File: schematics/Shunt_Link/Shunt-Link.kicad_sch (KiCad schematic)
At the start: 17 parts, among them IC1 AD8221TRMZ-EP, IC2 AD8221TRMZ-EP, IC3 AD8244ARMZ, J1 PCIe_1x_Bus, J2 Conn_01x05_Socket

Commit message: Updated to git
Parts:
- removed D1: LED_Lights, APT_Needs:LED_Lights, symbol APT_Needs:LED_Lights
- removed IC1, IC2: AD8221TRMZ-EP, APT_Needs:AD8221TRMZ-EP, symbol APT_Needs:AD8221TRMZ-EP
- removed IC3: AD8244ARMZ, APT_Needs:AD8244ARMZ, symbol APT_Needs:AD8244ARMZ
- removed J1: PCIe_1x_Bus, Connector_PCBEdge:BUS_PCIexpress_x1, symbol APT_Needs:PCIe_1x_Bus
- removed TP1, TP2, TP3: Keystone_1045, APT_Needs:Keystone_1045, symbol APT_Needs:Keystone_1045
- added D1: WP130WCP_2EGW, Link_Footprints:LED_Lights, symbol Link_Components:WP130WCP_2EGW
- added IC1, IC2: AD8221TRMZ-EP, Link_Footprints:AD8221TRMZ-EP, symbol Link_Components:AD8221TRMZ-EP
- added J1: PCIE-036-02-X-D-TH, Link_Footprints:SAMTEC_PCIE_1x, symbol Link_Components:PCIE-036-02-X-D-TH
- added L1: AD8244ARMZ, Link_Footprints:AD8244ARMZ, symbol Link_Components:AD8244ARMZ
- added TP1, TP2, TP3: 1045, Link_Footprints:Keystone_1045, symbol Link_Components:1045
- J2: footprint APT_Needs:Phoenix_Contact_MSTBA-LR -> Link_Footprints:Phoenix_Contact_MSTBA,5-LR
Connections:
- net GND: now also D1.2, D1.5, IC1.4 (+IN), IC1.5 (-VS), IC2.4 (+IN), IC2.5 (-VS), J1.B18, L1.8 (-VS), TP3.TP1
- net Green_{1}: now also D1.3, J1.B10
- net Green_{2}: now also D1.6, J1.B12
- net Red_{1}: now also D1.1, J1.B11
- net Red_{2}: now also D1.4, J1.B13
- net S_{+}: now also IC1.1 (-IN)
- net S_{o}: now also IC1.7 (VOUT), J1.B1, L1.6 (INC)
- net S_{test}: now also L1.7 (OUTC), TP1.TP1
- net T_{+}: now also IC2.1 (-IN)
- net T_{o}: now also IC2.7 (VOUT), J1.B2, L1.10 (IND)
- net T_{test}: now also L1.9 (OUTD), TP2.TP1
- net V_{+}: now also L1.4 (OUTB)
- net V_{2.5}: now also L1.1 (INA)
- net V_{5}: now also L1.5 (INB)
- net V_{ref}: now also IC1.6 (REF), IC2.6 (REF), L1.2 (OUTA)
- net V_{s}: now also IC1.8 (+VS), IC2.8 (+VS), J1.B17, L1.3 (+VS)
- net at Rg_2.1: now also IC2.2 (RG_1)
- net at Rg_2.2: now also IC2.3 (RG_2)
- net at Rg_1.1: now also IC1.2 (RG_1)
- net at Rg_1.2: now also IC1.3 (RG_2)
- new net NC: J1.A1, J1.A10, J1.A11, J1.A12, J1.A13, J1.A14, J1.A15, J1.A16, J1.A17, J1.A18, J1.A2, J1.A3, J1.A4, J1.A5, J1.A6, J1.A7, J1.A8, J1.A9, J1.B14, J1.B15, J1.B16, J1.B3, J1.B4, J1.B5, J1.B6, J1.B7, J1.B8, J1.B9

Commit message: started straing gauge link, updated shunt-link:
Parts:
- added C1: 0.1 uF, symbol Device:C
- added C2: 10 uF, symbol Device:C_US
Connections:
- net GND: now also C1.2, C2.2
- net V_{s}: now also C1.1, C2.1
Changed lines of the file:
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@@
 	(paper "A4")
+	(junction
+		(at 151.13 31.75)
+		(diameter 0)
+		(color 0 0 0 0)
+	)
 	(junction
 		(at 85.09 39.37)
@@
 	)
 	(junction
+		(at 165.1 31.75)
+		(diameter 0)
+		(color 0 0 0 0)
+	)
+	(junction
 		(at 93.98 118.11)
+		(diameter 0)
+		(color 0 0 0 0)
+	)
+	(junction
+		(at 151.13 39.37)
+		(diameter 0)
+		(color 0 0 0 0)
+	)
+	(junction
+		(at 165.1 39.37)
 		(diameter 0)
 		(color 0 0 0 0)
@@
 	(wire
 		(pts
-			(xy 132.08 39.37) (xy 138.43 39.37)
-		)
-		(stroke
-			(width 0)
-			(type default)
-		)
-	)
-	(wire
-		(pts
 			(xy 147.32 134.62) (xy 152.4 134.62)
 		)
@@
 	(wire
 		(pts
+			(xy 172.72 39.37) (xy 165.1 39.37)
+		)
+		(stroke
+			(width 0)
+			(type default)
+		)
+	)
+	(wire
+		(pts
 			(xy 73.66 40.64) (xy 85.09 40.64)
 		)
@@
 	(wire
 		(pts
+			(xy 151.13 31.75) (xy 165.1 31.75)
+		)
+		(stroke
+			(width 0)
+			(type default)
+		)
+	)
+	(wire
+		(pts
 			(xy 86.36 54.61) (xy 86.36 53.34)
 		)
@@
 	(wire
 		(pts
+			(xy 132.08 31.75) (xy 151.13 31.75)
+		)
+		(stroke
+			(width 0)
+			(type default)
+		)
+	)
+	(wire
+		(pts
 			(xy 76.2 118.11) (xy 76.2 120.65)
 		)
@@
 	(wire
 		(pts
+			(xy 132.08 39.37) (xy 151.13 39.37)
+		)
+		(stroke
+			(width 0)
+			(type default)
+		)
+	)
+	(wire
+		(pts
 			(xy 102.87 36.83) (xy 104.14 36.83)
 		)
@@
 	(wire
 		(pts
+			(xy 165.1 39.37) (xy 151.13 39.37)
+		)
+		(stroke
+			(width 0)
+			(type default)
+		)
+	)
+	(wire
+		(pts
 			(xy 116.84 111.76) (xy 121.92 111.76)
 		)
@@
 	(wire
 		(pts
+			(xy 165.1 31.75) (xy 172.72 31.75)
+		)
+		(stroke
+			(width 0)
+			(type default)
+		)
+	)
+	(wire
+		(pts
 			(xy 116.84 114.3) (xy 121.92 114.3)
 		)
@@
 	(wire
 		(pts
-			(xy 132.08 31.75) (xy 138.43 31.75)
-		)
-		(stroke
-			(width 0)
-			(type default)
-		)
-	)
-	(wire
-		(pts
 			(xy 93.98 118.11) (xy 93.98 120.65)
 		)
@@
 	(label "NC"
 		(at 116.84 129.54 0)
+		(effects
+			(font
+				(size 1.27 1.27)
+			)
+			(justify left bottom)
+		)
+	)
+	(label "GND"
+		(at 172.72 39.37 0)
 		(effects
 			(font
@@
 		)
 	)
+	(label "V_{s}"
+		(at 172.72 31.75 0)
+		(effects
+			(font
+				(size 1.27 1.27)
+			)
+			(justify left bottom)
+		)
+	)
 	(label "T_{test}"
 		(at 139.7 78.74 0)
@@
 		)
 	)
-	(label "GND"
-		(at 138.43 39.37 0)
-		(effects
-			(font
-				(size 1.27 1.27)
-			)
-			(justify left bottom)
-		)
-	)
 	(label "NC"
 		(at 116.84 121.92 0)
-		(effects
-			(font
-				(size 1.27 1.27)
-			)
-			(justify left bottom)
-		)
-	)
-	(label "V_{s}"
-		(at 138.43 31.75 0)
 		(effects
 			(font
@@
 			)
 			(justify left bottom)
+		)
+	)
+	(symbol
+		(lib_id "Device:C_US")
+		(at 165.1 35.56 0)
+		(unit 1)
+		(exclude_from_sim no)
+		(in_bom yes)
+		(on_board yes)
+		(dnp no)
+		(property "Reference" "C2"
+			(at 168.91 33.528 0)
+			(effects
+				(font
+					(size 1.27 1.27)
+				)
+				(justify left)
+			)
+		)
+		(property "Value" "10 uF"
+			(at 168.91 36.068 0)
+			(effects
+				(font
+					(size 1.27 1.27)
+				)
+				(justify left)
+			)
+		)
+		(property "Footprint" ""
+			(at 165.1 35.56 0)
+			(effects
+				(font
+					(size 1.27 1.27)
+				)
+				(hide yes)
+			)
+		)
+		(property "Datasheet" ""
+			(at 165.1 35.56 0)
+			(effects
+				(font
+					(size 1.27 1.27)
+				)
+				(hide yes)
+			)
+		)
+		(property "Description" "capacitor, US symbol"
+			(at 165.1 35.56 0)
+			(effects
+				(font
+					(size 1.27 1.27)
+				)
+				(hide yes)
+			)
+		)
+		(pin "1"
+		)
+		(pin "2"
+		)
+		(instances
+			(project "Shunt-Link"
+				(path "/044df771-0288-4dc4-a604-257e905d1378"
+					(reference "C2")
+					(unit 1)
+				)
+			)
 		)
 	)
@@
 					(unit 1)
 				)
+			)
+		)
+	)
+	(symbol
+		(lib_id "Device:C")
+		(at 151.13 35.56 0)
+		(unit 1)
+		(exclude_from_sim no)
+		(in_bom yes)
+		(on_board yes)
+		(dnp no)
+		(fields_autoplaced yes)
+		(property "Reference" "C1"
+			(at 154.94 34.2899 0)
+			(effects
+				(font
+					(size 1.27 1.27)
+				)
+				(justify left)
+			)
+		)
+		(property "Value" "0.1 uF"
+			(at 154.94 36.8299 0)
+			(effects
+				(font
+					(size 1.27 1.27)
+				)
+				(justify left)
+			)
+		)
+		(property "Footprint" ""
+			(at 152.0952 39.37 0)
+			(effects
+				(font
+					(size 1.27 1.27)
+				)
+				(hide yes)
+			)
+		)
+		(property "Datasheet" "~"
+			(at 151.13 35.56 0)
+			(effects
+				(font
+					(size 1.27 1.27)
+				)
+				(hide yes)
+			)
+		)
+		(property "Description" "Unpolarized capacitor"
+			(at 151.13 35.56 0)
+			(effects
+				(font
+					(size 1.27 1.27)
+				)
+				(hide yes)
+			)
+		)
+		(pin "2"
+		)
+		(pin "1"
+		)
+		(instances
+			(project "Shunt-Link"
+				(path "/044df771-0288-4dc4-a604-257e905d1378"
+					(reference "C1")
+					(unit 1)
+				)

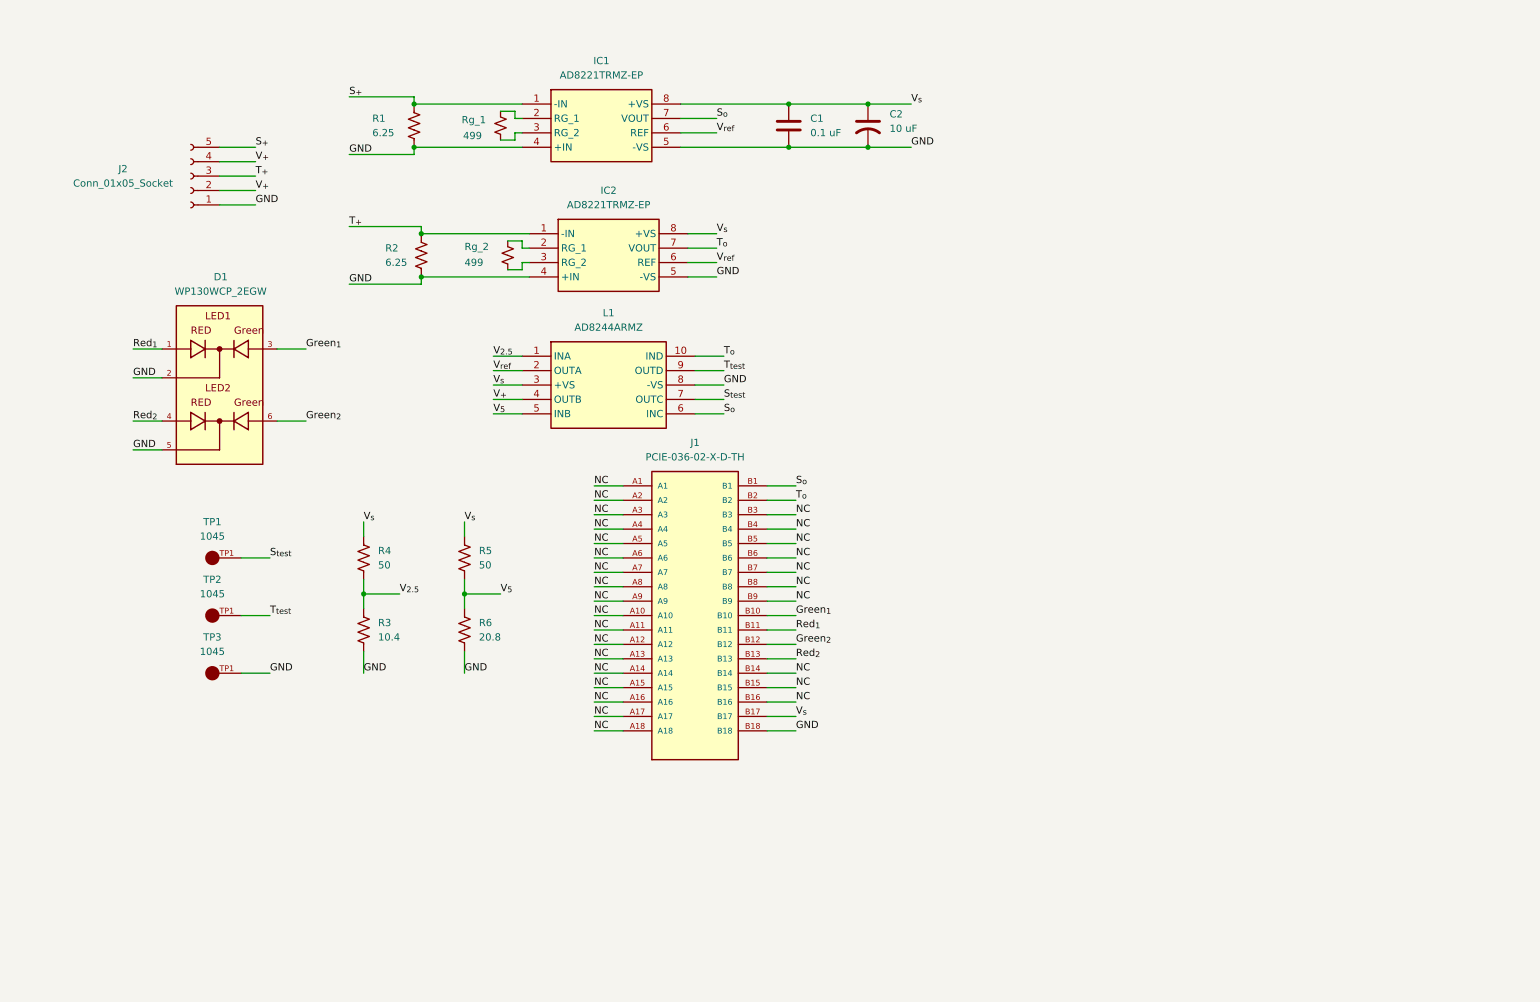
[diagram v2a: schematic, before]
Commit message: Changed V Labels, remove extra pins for now
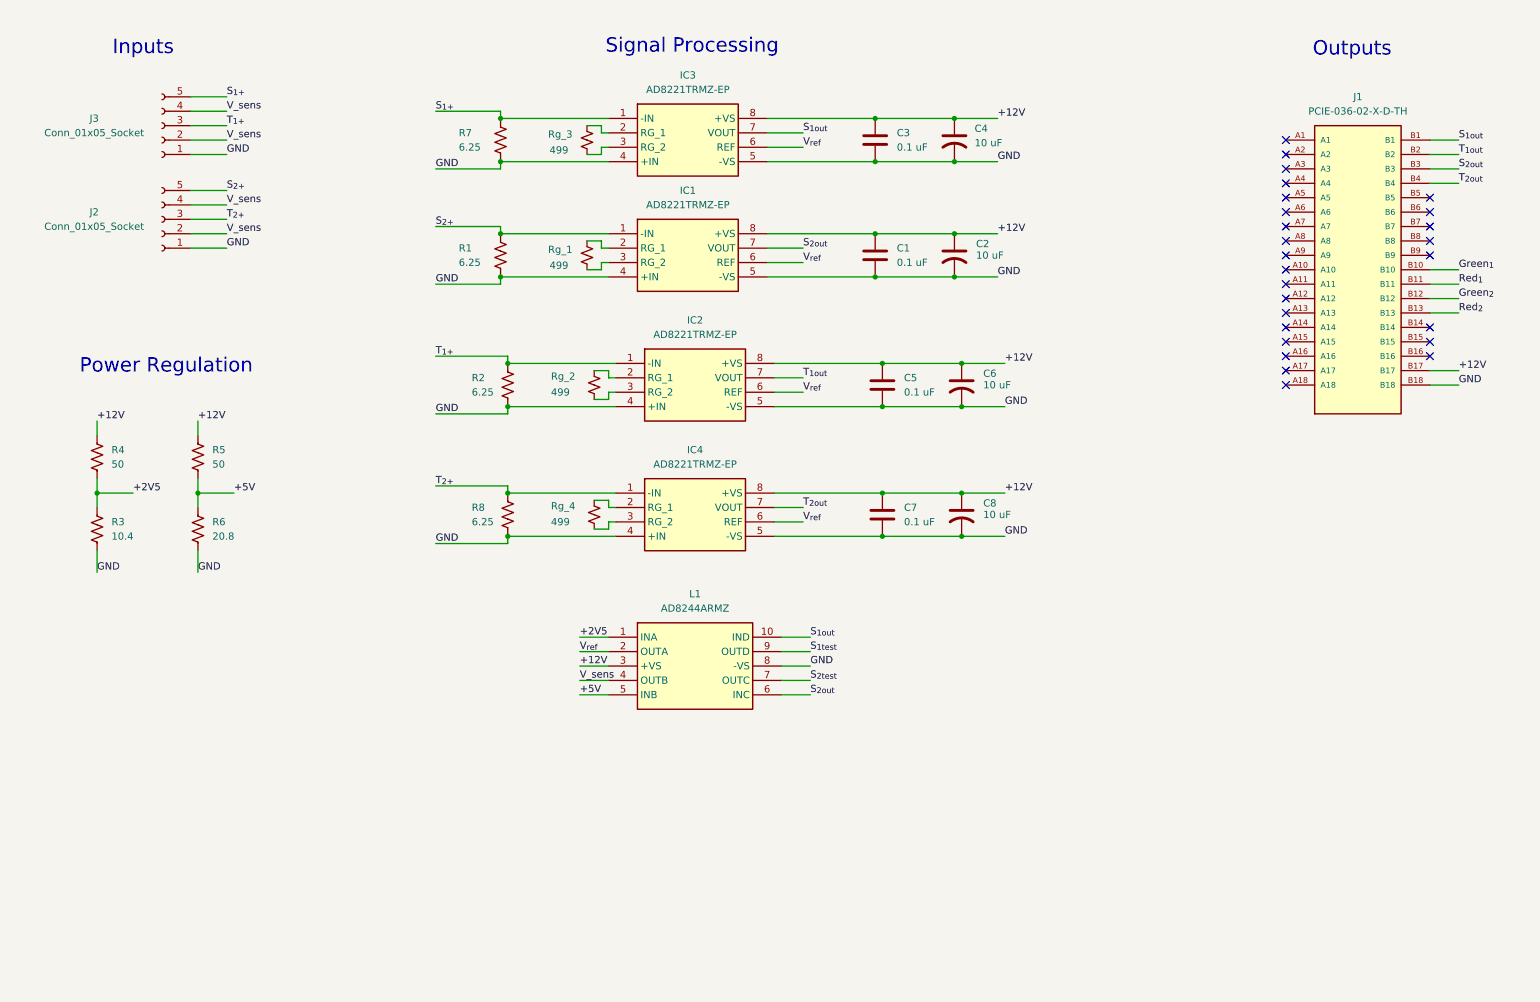
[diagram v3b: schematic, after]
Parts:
- removed D1: WP130WCP_2EGW, Link_Footprints:LED_Lights, symbol Link_Components:WP130WCP_2EGW
- removed TP1, TP2, TP3: 1045, Link_Footprints:Keystone_1045, symbol Link_Components:1045
- added C3, C5, C7: 0.1 uF, Capacitor_SMD:C_1210_3225Metric, symbol Device:C
- added C4, C6, C8: 10 uF, Capacitor_SMD:C_1210_3225Metric, symbol Device:C_US
- added IC3, IC4: AD8221TRMZ-EP, Link_Footprints:AD8221TRMZ-EP, symbol Link_Components:AD8221TRMZ-EP
- added J3: Conn_01x05_Socket, Link_Footprints:Phoenix_Contact_MSTBA,5-LR, symbol Connector:Conn_01x05_Socket
- added R7, R8: 6.25, Resistor_SMD:R_0805_2012Metric, symbol Device:R_US
- added Rg_3, Rg_4: 499, Resistor_SMD:R_0805_2012Metric, symbol Device:R_Small_US
- C1, C2: footprint (none) -> Capacitor_SMD:C_1210_3225Metric
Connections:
- net GND: now also C3.2, C4.2, C5.2, C6.2, C7.2, C8.2, IC3.4 (+IN), IC3.5 (-VS), IC4.4 (+IN), IC4.5 (-VS), J3.1 (Pin_1), R7.2, R8.2
- net V_{ref}: now also IC3.6 (REF), IC4.6 (REF)
- removed net NC: J1.A1, J1.A10, J1.A11, J1.A12, J1.A13, J1.A14, J1.A15, J1.A16, J1.A17, J1.A18, J1.A2, J1.A3, J1.A4, J1.A5, J1.A6, J1.A7, J1.A8, J1.A9, J1.B14, J1.B15, J1.B16, J1.B3, J1.B4, J1.B5, J1.B6, J1.B7, J1.B8, J1.B9
- net S_{+} renamed S_{2+}
- net S_{o} renamed S_{2out}
- net S_{2out}: now also J1.B3; no longer J1.B1
- net S_{test} renamed S_{2test}
- net T_{+} renamed T_{1+}
- net T_{1+}: now also J3.3 (Pin_3); no longer J2.3 (Pin_3)
- net T_{o} renamed T_{1out}
- net T_{1out}: no longer L1.10 (IND)
- net T_{test} renamed S_{1test}
- net V_{+} renamed V_sens
- net V_sens: now also J3.2 (Pin_2), J3.4 (Pin_4)
- net V_{2.5} renamed +2V5
- net V_{5} renamed +5V
- net V_{s} renamed +12V
- net +12V: now also C3.1, C4.1, C5.1, C6.1, C7.1, C8.1, IC3.8 (+VS), IC4.8 (+VS)
- new net: IC3.2 (RG_1), Rg_3.1
- new net: IC3.3 (RG_2), Rg_3.2
- new net: IC4.2 (RG_1), Rg_4.1
- new net: IC4.3 (RG_2), Rg_4.2
- new net S_{1+}: IC3.1 (-IN), J3.5 (Pin_5), R7.1
- new net S_{1out}: IC3.7 (VOUT), J1.B1, L1.10 (IND)
- new net T_{2+}: IC4.1 (-IN), J2.3 (Pin_3), R8.1
- new net T_{2out}: IC4.7 (VOUT), J1.B4
- no-connect marks 0 -> 26
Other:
- note added: "Inputs"
- note added: "Outputs"
- note added: "Power Regulation"
- note added: "Signal Processing"
- moved on the sheet: C1, C2, IC1, IC2, J1, J2, L1, R1, R2, R3, R4, R5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

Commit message: Added regulators to Shunt_Link, Edited lib
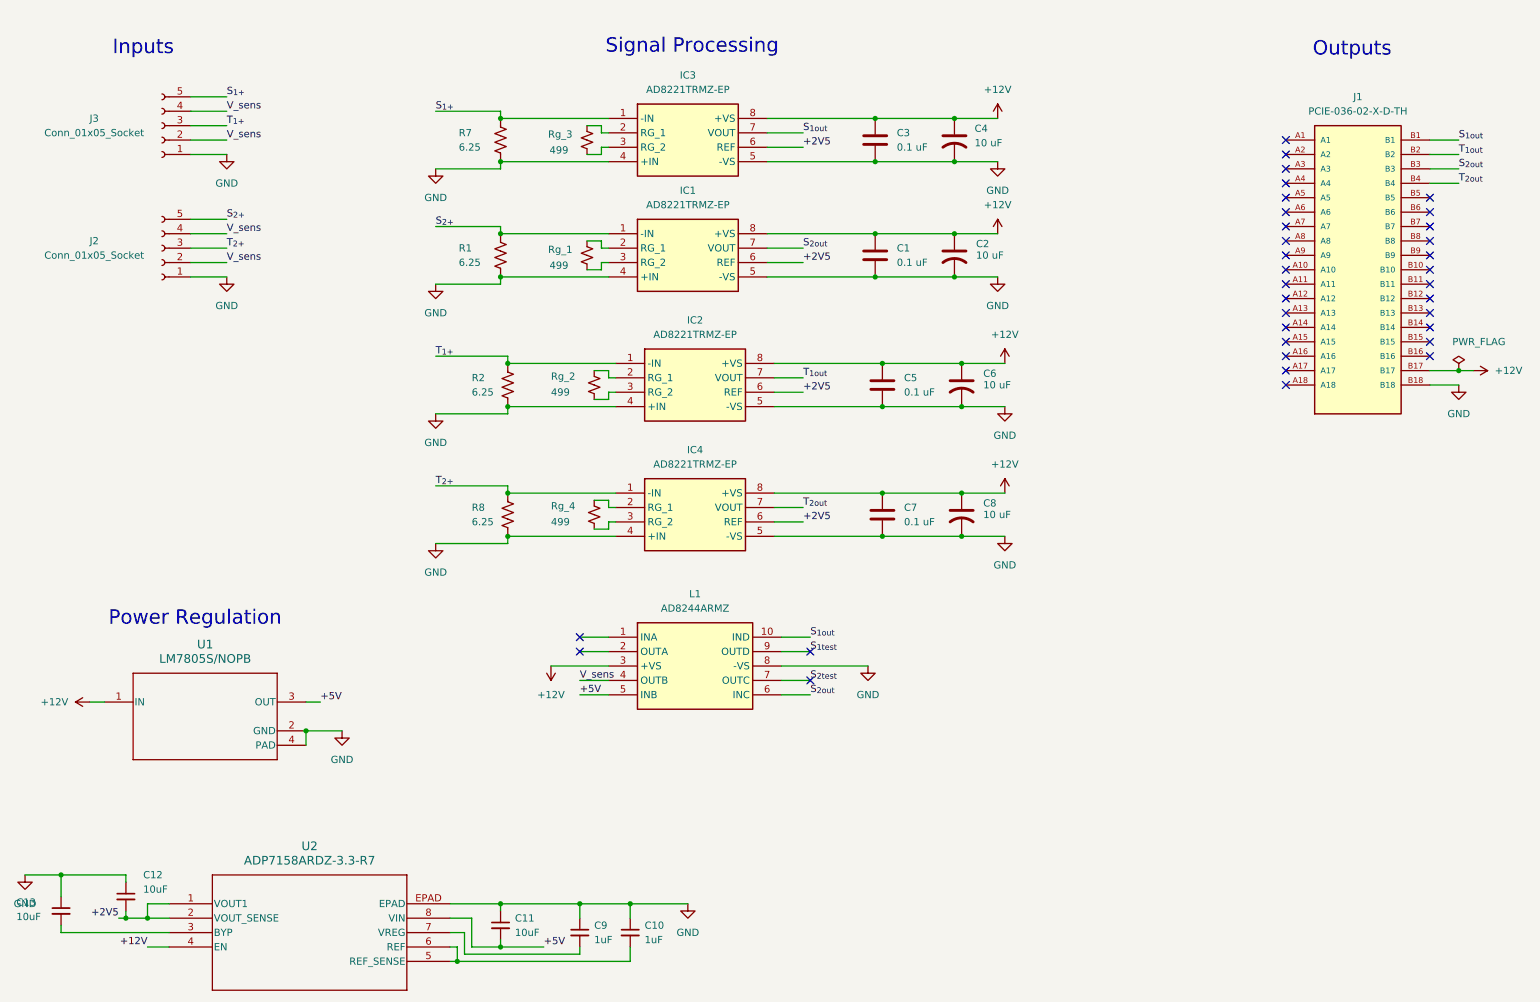
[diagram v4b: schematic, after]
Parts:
- removed R3: 10.4, Resistor_SMD:R_0805_2012Metric, symbol Device:R_US
- removed R4, R5: 50, Resistor_SMD:R_0805_2012Metric, symbol Device:R_US
- removed R6: 20.8, Resistor_SMD:R_0805_2012Metric, symbol Device:R_US
- added C10, C9: 1uF, symbol Device:C_Small
- added C11, C12, C13: 10uF, symbol Device:C_Small
- added U1: LM7805S/NOPB, KTT0003B_N, symbol Link_Components:LM7805S_NOPB
- added U2: ADP7158ARDZ-3.3-R7, ADP7158ARDZ-3.3-R7_ADI, symbol Link_Components:ADP7158ARDZ-3.3-R7
- J1: footprint Link_Footprints:SAMTEC_PCIE_1x -> (none)
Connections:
- net +12V: now also U1.1 (IN), U2.4 (EN)
- net +2V5: now also IC1.6 (REF), IC2.6 (REF), IC3.6 (REF), IC4.6 (REF), C12.2, U2.1 (VOUT1), U2.2 (VOUT_SENSE); no longer L1.1 (INA)
- net +5V: now also C11.2, U1.3 (OUT), U2.8 (VIN)
- net GND: now also C10.1, C11.1, C12.1, C13.1, C9.1, U1.2 (GND), U1.4 (PAD), U2.EPAD
- net Green_{1}: no longer names the net of J1.B10
- net Green_{2}: no longer names the net of J1.B12
- net Red_{1}: no longer names the net of J1.B11
- net Red_{2}: no longer names the net of J1.B13
- removed net V_{ref}: IC1.6 (REF), IC2.6 (REF), IC3.6 (REF), IC4.6 (REF), L1.2 (OUTA)
- new net: C13.2, U2.3 (BYP)
- new net: C10.2, U2.5 (REF_SENSE), U2.6 (REF)
- new net: C9.2, U2.7 (VREG)
- no-connect marks 26 -> 34
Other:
- moved on the sheet: J2
